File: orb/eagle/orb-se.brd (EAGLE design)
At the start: 86.8 x 80.9 mm, 27 parts, among them J1 MICRO USB, Q1 12MHZ, T1 DMG2302U, T2 DMG2302U, T3 DMG2302U, U1 ATINY44A

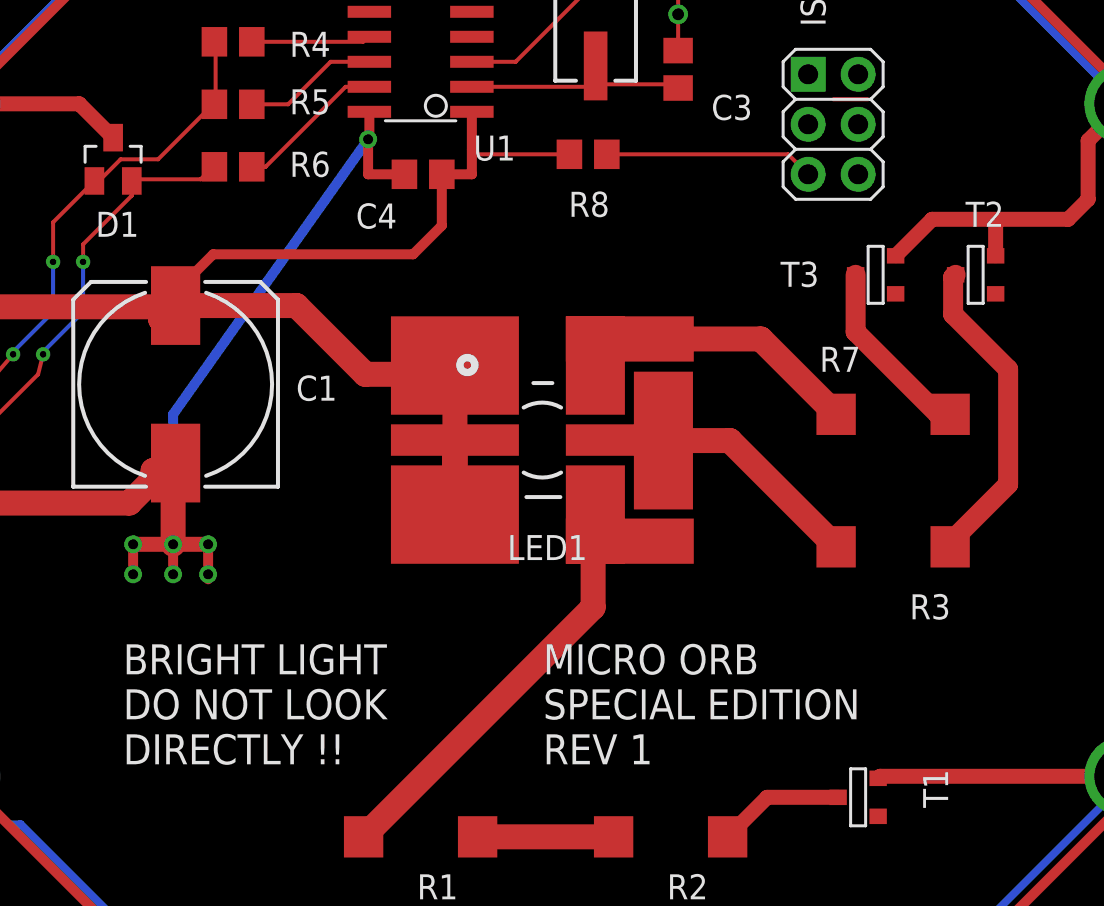
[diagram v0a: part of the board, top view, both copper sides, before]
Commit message: Minor tweaks. Cleaned DRC errors. Verified netlist. Ready for final auto routing.
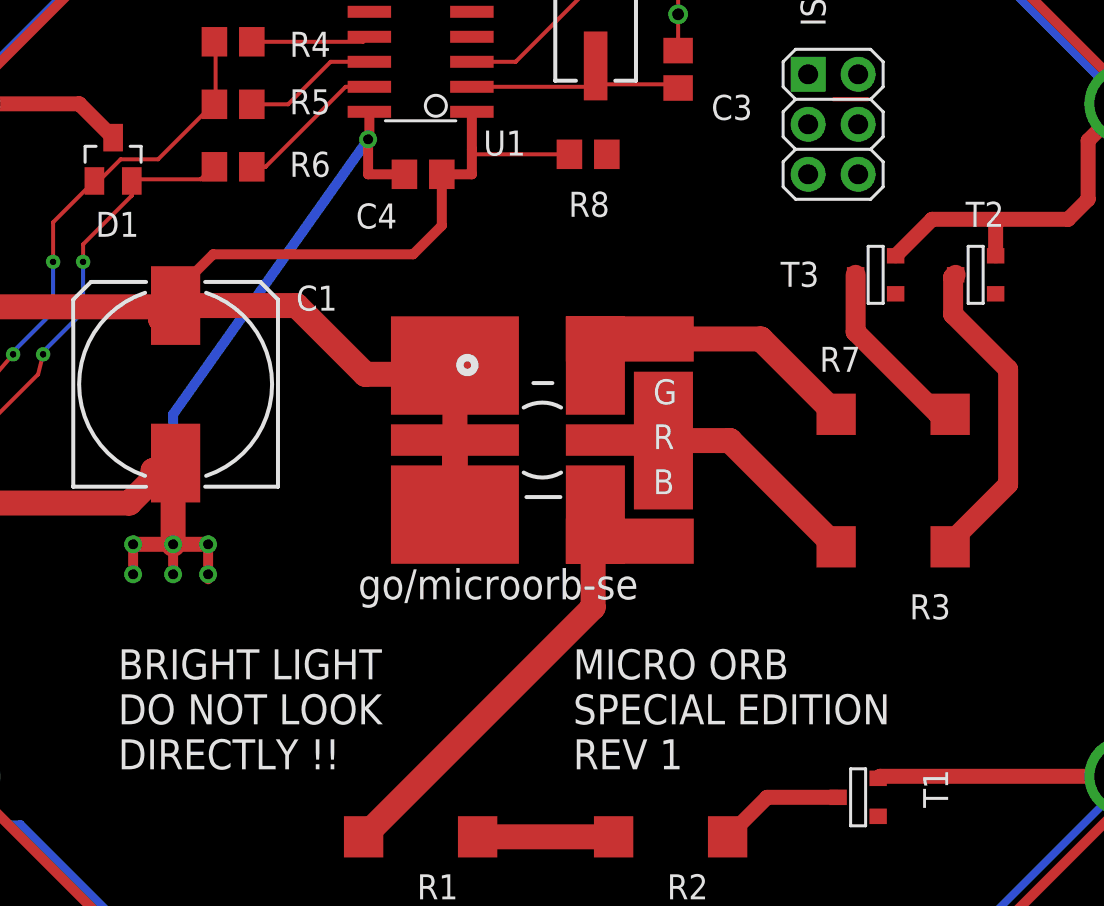
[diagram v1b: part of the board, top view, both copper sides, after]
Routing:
- net RESET: track 11.3 -> 0.63 mm
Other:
- board text added: "B"
- board text added: "G"
- board text added: "R"
- board text added: "go/microorb-se"
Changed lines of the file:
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@@
 <circle x="50" y="50" radius="40.165" width="0.0254" layer="48"/>
 <circle x="50" y="50" radius="35" width="12" layer="30"/>
-<text x="50.038" y="33.528" size="1.524" layer="21" font="vector" ratio="10">MICRO ORB
+<text x="51.562" y="33.274" size="1.524" layer="21" font="vector" ratio="10">MICRO ORB
 SPECIAL EDITION
 REV 1</text>
-<text x="28.702" y="33.528" size="1.524" layer="21" font="vector" ratio="10">BRIGHT LIGHT
+<text x="28.448" y="33.274" size="1.524" layer="21" font="vector" ratio="10">BRIGHT LIGHT
 DO NOT LOOK
 DIRECTLY !!</text>
+<text x="55.626" y="51.816" size="1.27" layer="21" font="vector" ratio="10">G</text>
+<text x="55.626" y="49.53" size="1.27" layer="21" font="vector" ratio="10">R</text>
+<text x="55.626" y="47.244" size="1.27" layer="21" font="vector" ratio="10">B</text>
+<text x="40.64" y="41.91" size="1.524" layer="21" font="vector" ratio="10">go/microorb-se</text>
 </plain>
 <attributes>
@@
 <element name="MH$6" library="orb-se" package="MOUNTING_HOLE" value="MOUNTING_HOLE" x="20.41" y="32.92" smashed="yes"/>
 <element name="U1" library="orb-se" package="SOIC14" value="ATINY44A" x="43.815" y="70.485" smashed="yes" rot="R90">
-<attribute name="NAME" x="48.641" y="65.4685" size="1.27" layer="25" font="vector" ratio="10" rot="R180"/>
+<attribute name="NAME" x="49.149" y="65.7225" size="1.27" layer="25" font="vector" ratio="10" rot="R180"/>
 </element>
 <element name="D1" library="orb-se" package="SOT23" value="AZ23C3V6" x="28.194" y="64.262" smashed="yes">
@@
 </element>
 <element name="C1" library="orb-se" package="153CLV-1010" value="1000U 10V" x="31.369" y="52.832" smashed="yes" rot="R90">
-<attribute name="NAME" x="39.58" y="53.271" size="1.27" layer="25" font="vector" rot="R180"/>
-</element>
-<element name="LED1" library="orb-se" package="OVSTRGBBCR4" value="OVSTRGBBCR4" x="50" y="50" smashed="yes">
-<attribute name="NAME" x="48.222" y="43.904" size="1.27" layer="25" font="vector"/>
-</element>
+<attribute name="NAME" x="39.58" y="57.843" size="1.27" layer="25" font="vector" rot="R180"/>
+</element>
+<element name="LED1" library="orb-se" package="OVSTRGBBCR4" value="OVSTRGBBCR4" x="50" y="50" smashed="yes"/>
 <element name="R1" library="orb-se" package="R2512W" value="10R 1W" x="43.815" y="29.845" smashed="yes" rot="R180">
 <attribute name="NAME" x="45.72" y="27.94" size="1.27" layer="25" font="vector" rot="R180"/>
@@
 <contactref element="R8" pad="1"/>
 <contactref element="U1" pad="4"/>
-<wire x1="62.484" y1="64.516" x2="53.274" y2="64.516" width="0.2032" layer="1"/>
-<wire x1="63.5" y1="63.5" x2="62.484" y2="64.516" width="0.2032" layer="1"/>
+<wire x1="62.484" y1="64.516" x2="53.274" y2="64.516" width="0" layer="19" extent="1-16"/>
+<wire x1="63.5" y1="63.5" x2="62.484" y2="64.516" width="0" layer="19" extent="1-16"/>
 <wire x1="45.847" y1="70.485" x2="46.4185" y2="70.485" width="0.2032" layer="1"/>
 <wire x1="53.213" y1="64.516" x2="53.274" y2="64.516" width="0.2032" layer="1"/>
@@
 </signal>
 </signals>
+<errors>
+</errors>
 </board>
 </drawing>

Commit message: Done final routing.
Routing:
- net SCK/BLUE: track 0.00 -> 61.8 mm, vias 0 -> 1
- net MISO/GREEN: track 1.78 -> 47.2 mm
- net MOSI/RED: track 0.10 -> 37.8 mm, vias 0 -> 2
- net RESET: track 0.63 -> 31.8 mm, vias 0 -> 1
- net +5V: track 82.5 -> 104.3 mm
- net DP: track 9.05 -> 16.8 mm
- net GND: track 561.3 -> 563.1 mm
- net N$1: track 15.1 -> 16.2 mm
- net N$7: track 22.0 -> 22.9 mm
